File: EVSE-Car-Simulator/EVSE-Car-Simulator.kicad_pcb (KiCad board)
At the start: 2 copper layers, 36.8 x 17.8 mm, 11 parts, among them J1 diode fault, J2 EV detect, J3 CP short, J4 EV ready, J5 Type 2, J6 CP-D, J7 PE-D

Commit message: completely routed, gerber files for production generated.
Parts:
- D1: value D -> 1N4007
- J5: value Type 2 -> Typ 2 Stecker
- moved R1 5.08 mm to (139.7, 109.2)
- moved R2 5.08 mm to (144.8, 109.2)
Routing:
- net Net-(J2-Pad1): track 0.00 -> 23.4 mm
- net Net-(J4-Pad1): track 0.00 -> 16.3 mm
- net CP: track 65.4 -> 52.8 mm
- added copper zone on F.Cu, net PE
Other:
- board text added: "EVsim v0.1 Mathias Dalheimer"

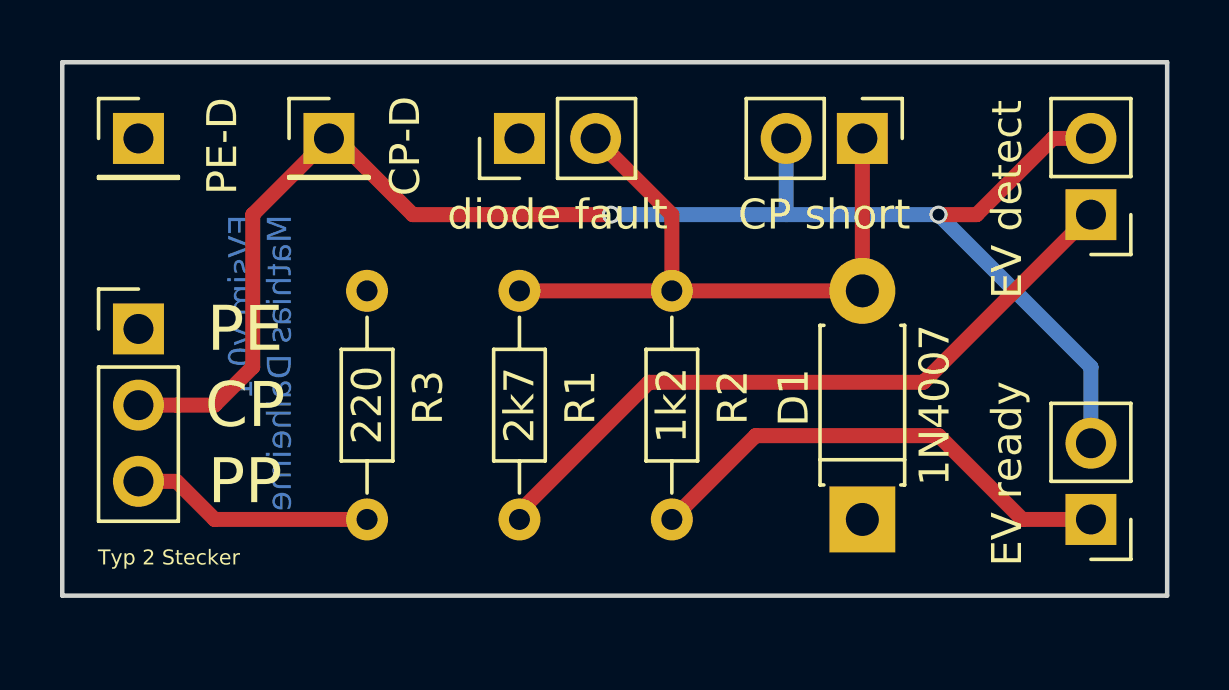
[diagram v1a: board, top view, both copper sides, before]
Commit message: increased hole size for type2 connector, rerouted to make enough room
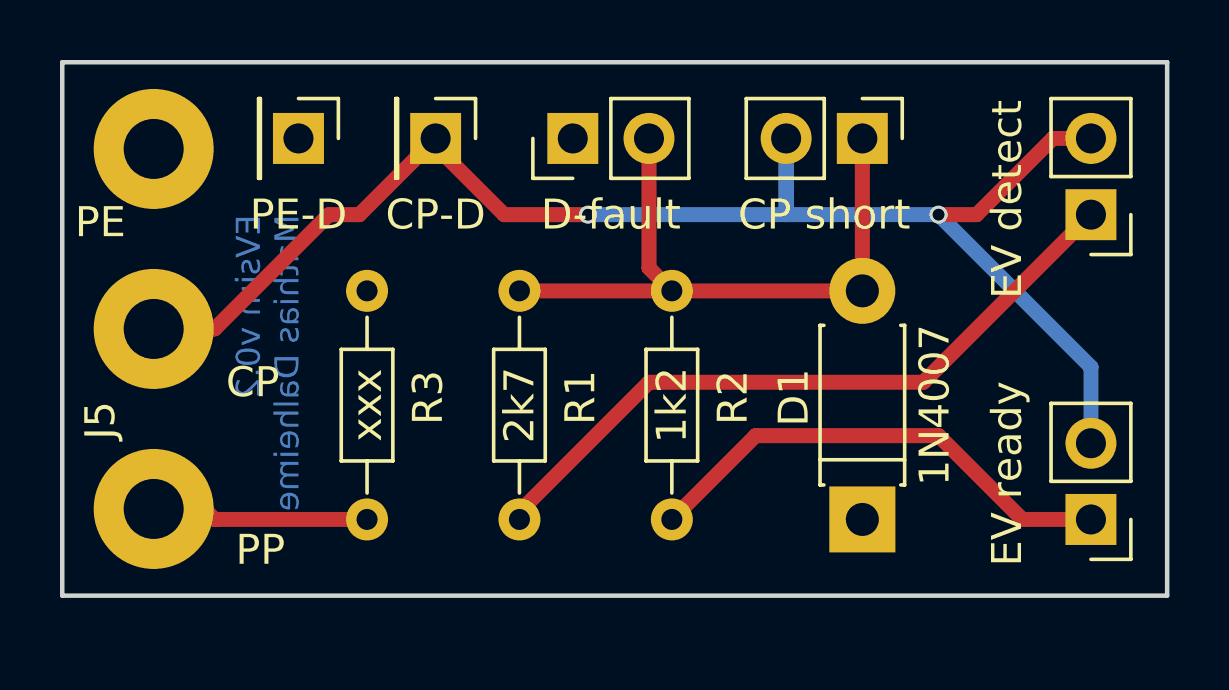
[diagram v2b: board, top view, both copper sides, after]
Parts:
- J1: value diode fault -> D-fault
- J5: value Typ 2 Stecker -> Type 2; footprint Pin_Headers:Pin_Header_Straight_1x03_Pitch2.54mm -> lib:Type2-Solderpads
- R3: value 220 -> xxx
- moved J7 5.33 mm to (132.3, 96.5), turned to 270 degrees
- moved J6 3.56 mm to (136.9, 96.5), turned to 270 degrees
- moved J1 1.78 mm to (141.5, 96.5)
- moved J5 0.51 mm to (127.5, 102.9), turned to 270 degrees
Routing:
- net CP: track 52.8 -> 51.4 mm
- net N1: track 22.6 -> 21.9 mm, vias 0 -> 1
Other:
- board text added: "EVsim v0.2 Mathias Dalheimer"
- board text removed: "EVsim v0.1 Mathias Dalheimer"
